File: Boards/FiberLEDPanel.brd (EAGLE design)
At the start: 16.5 x 7.6 mm, 5 parts, among them U1 WS2812, U2 WS2812

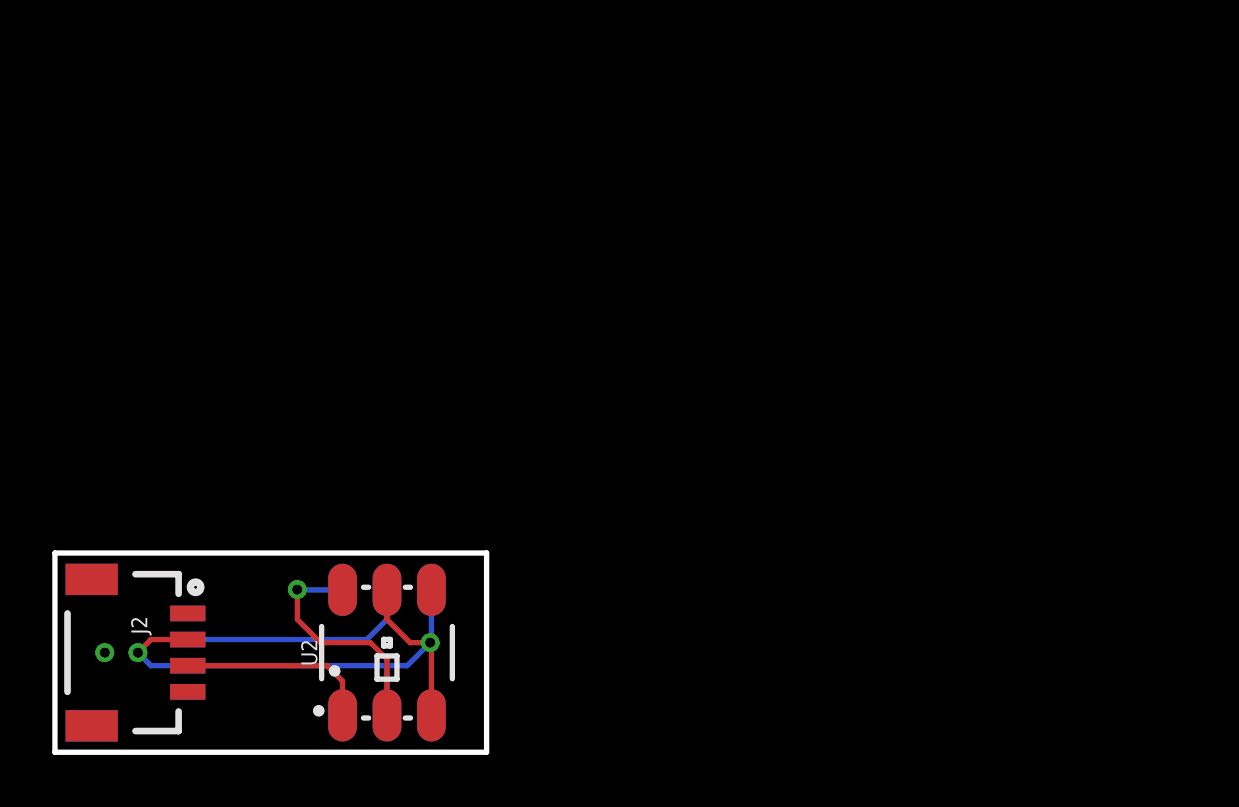
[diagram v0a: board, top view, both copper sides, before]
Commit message: added and ordered LEDs
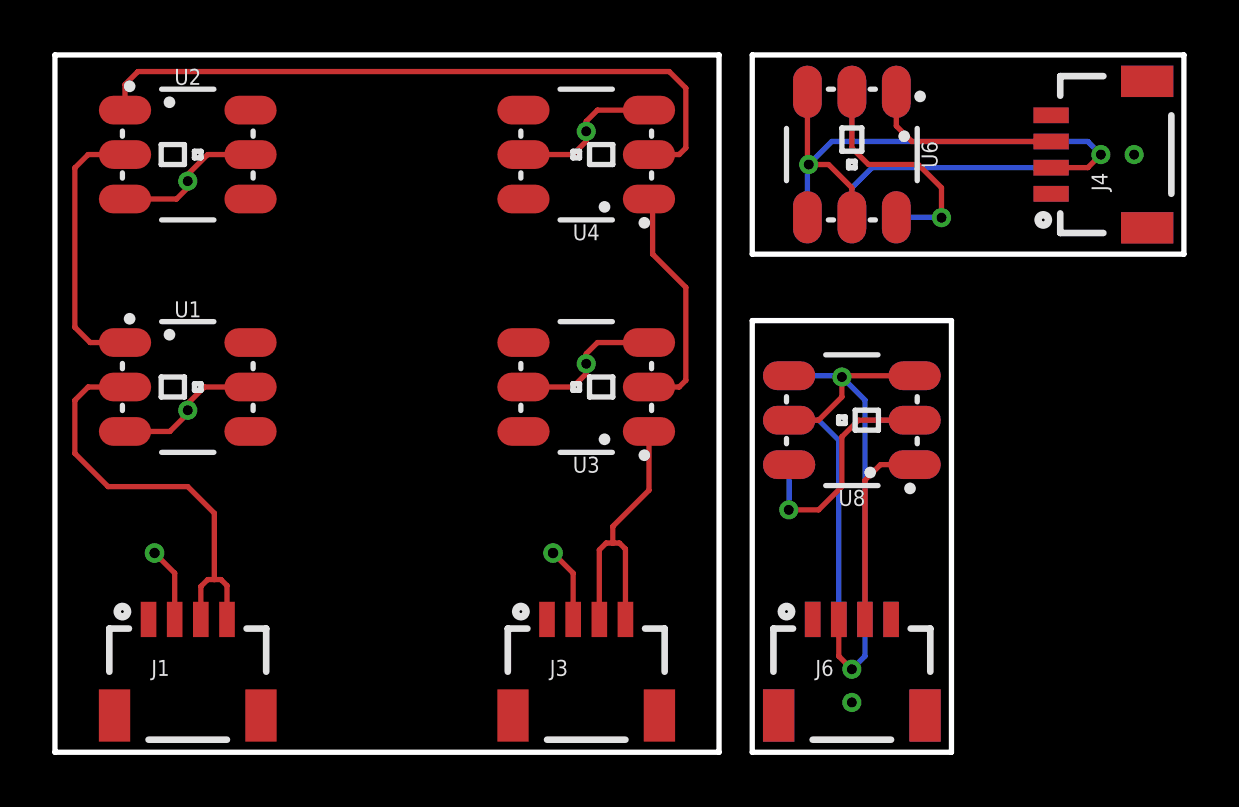
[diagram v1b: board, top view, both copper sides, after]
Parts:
- added FRAME2: FRAME-LETTER, SparkFun-Aesthetics:CREATIVE_COMMONS
- added J3, J4, J5, J6: (no value), SparkFun-Connectors:1X04_1MM_RA
- added U3, U4, U5, U6, U7, U8: WS2812, SparkFun-LED:LED-TRICOLOR-5050-IC
- moved J2 38.1 mm to (38.1, 22.9), flipped to the bottom
- moved U2 20.5 mm to (5.08, 22.9), turned to 0 degrees
- moved U1 12.7 mm to (5.08, 14.0), flipped to the top, turned to 0 degrees
- moved J1 1.27 mm to (5.08, 5.08), flipped to the top, turned to 0 degrees
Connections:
- new net 5V1: J2.2, J4.2, U5.3, U5.5, U6.3, U6.5
- new net 5V2: J5.2, J6.2, U7.3, U7.5, U8.3, U8.5
- new net GND1: J2.1, J4.1, U5.6, U6.6
- new net GND2: J5.1, J6.1, U7.6, U8.6
- new net N$10: J5.3, U7.2
- new net N$11: J6.3, U8.1
- new net N$2: U3.2, U4.1
- new net N$4: J3.3, J3.4, U3.1
- new net N$6: U5.1, U6.2
- new net N$7: J2.3, U5.2
- new net N$8: J4.3, U6.1
- new net N$9: U7.1, U8.2
- net 5V: now also J3.2, U3.3, U3.5, U4.3, U4.5; no longer J2.2
- net GND: now also J3.1, U3.6, U4.6; no longer J2.1
- net N$1: now also J1.4
- net N$3: now also U4.2; no longer J2.3
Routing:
- net 5V2: track 0.00 -> 23.7 mm, vias 0 -> 2
- net 5V1: track 0.00 -> 23.7 mm, vias 0 -> 2
- net N$3: track 7.47 -> 26.7 mm
- net N$4: track 0.00 -> 11.4 mm
- net N$6: track 0.00 -> 9.08 mm, vias 0 -> 1
- net N$9: track 0.00 -> 9.08 mm, vias 0 -> 1
- net N$10: track 0.00 -> 9.07 mm
- net N$7: track 0.00 -> 9.07 mm
- net N$2: track 0.00 -> 9.04 mm
- net N$1: track 9.07 -> 16.7 mm
- net N$8: track 0.00 -> 7.47 mm
- net N$11: track 0.00 -> 7.47 mm
- net 5V: track 23.7 -> 29.1 mm, vias 2 -> 6
- net N$5: track 9.08 -> 10.4 mm, vias 1 -> 0
- added copper zone on layer 16, net 5V
- added copper zone on layer 1, net GND1
- added copper zone on layer 16, net GND1
- added copper zone on layer 1, net GND2
- added copper zone on layer 16, net GND2
- removed copper zone on layer 16, net GND
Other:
- board size 16.5 x 7.6 mm -> 43.2 x 26.7 mm
